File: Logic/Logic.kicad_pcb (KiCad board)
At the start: 2 copper layers, 125.4 x 128.5 mm, 65 parts, among them IC1 RPi_Pico_SMD_TH, IC2 MC74ACT05DG, J1 PJ3410, J10 PinHeader_1x03_P2.54mm_Vertic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, J2 PJ3410, J3 PJ3410, J4 PJ3410, J5 PJ3410, J6 PJ3410, J7 PJ3410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

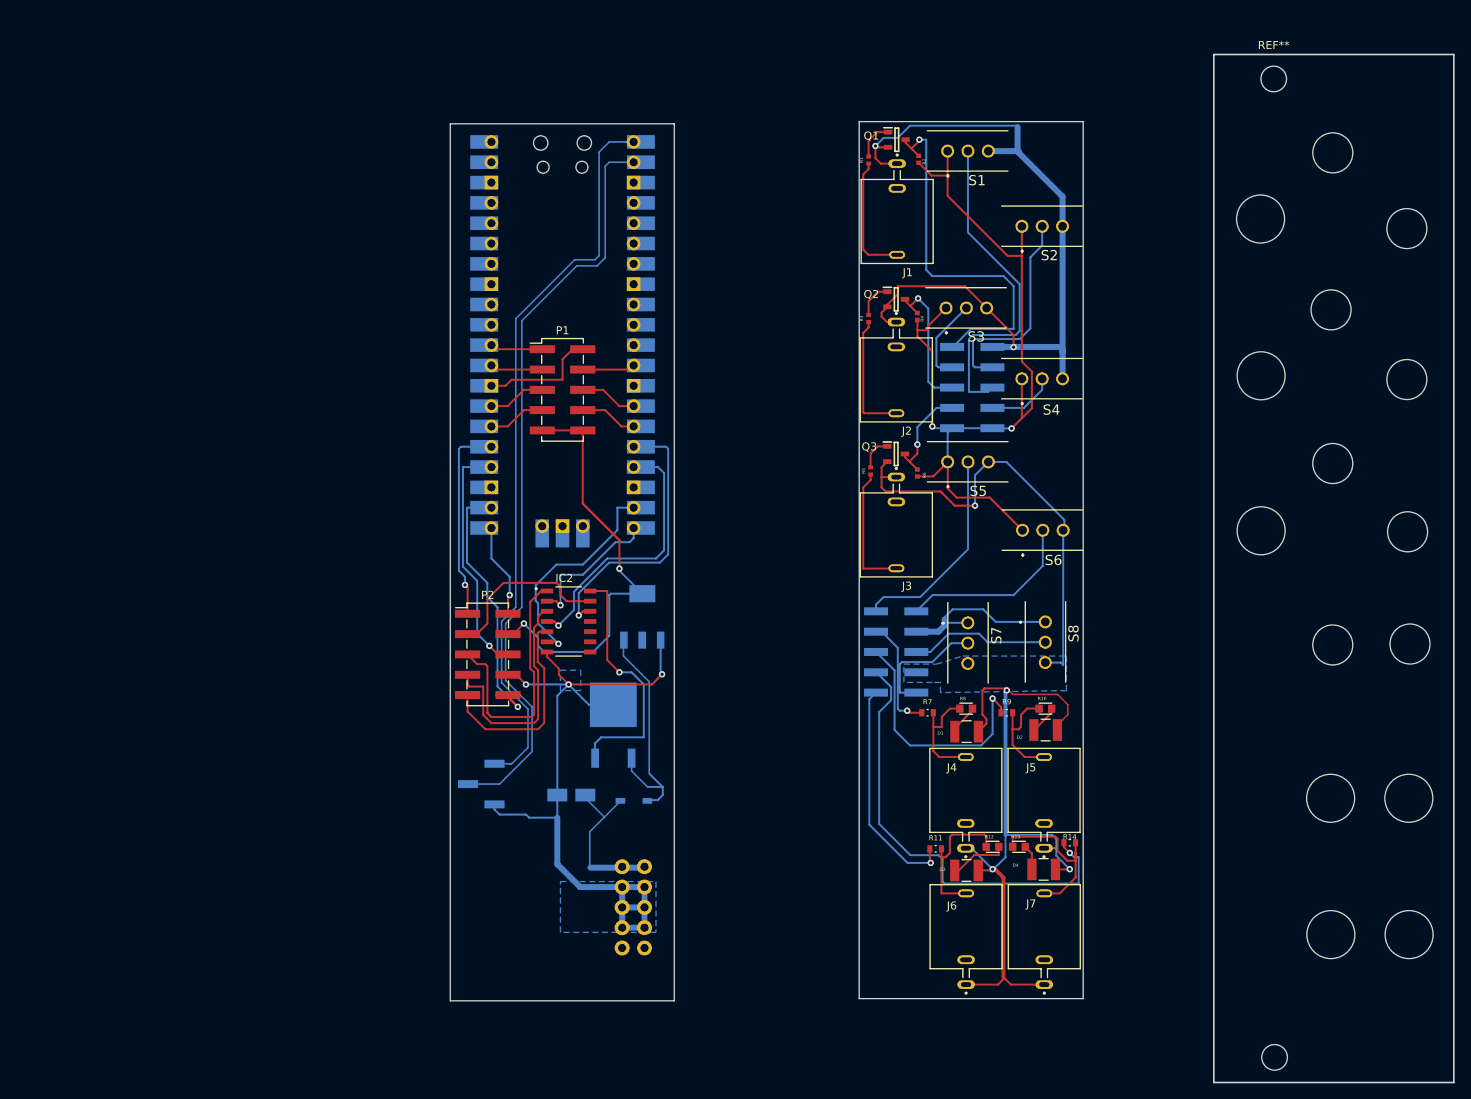
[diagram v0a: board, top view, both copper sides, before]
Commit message: Input LEDs and other tweaks
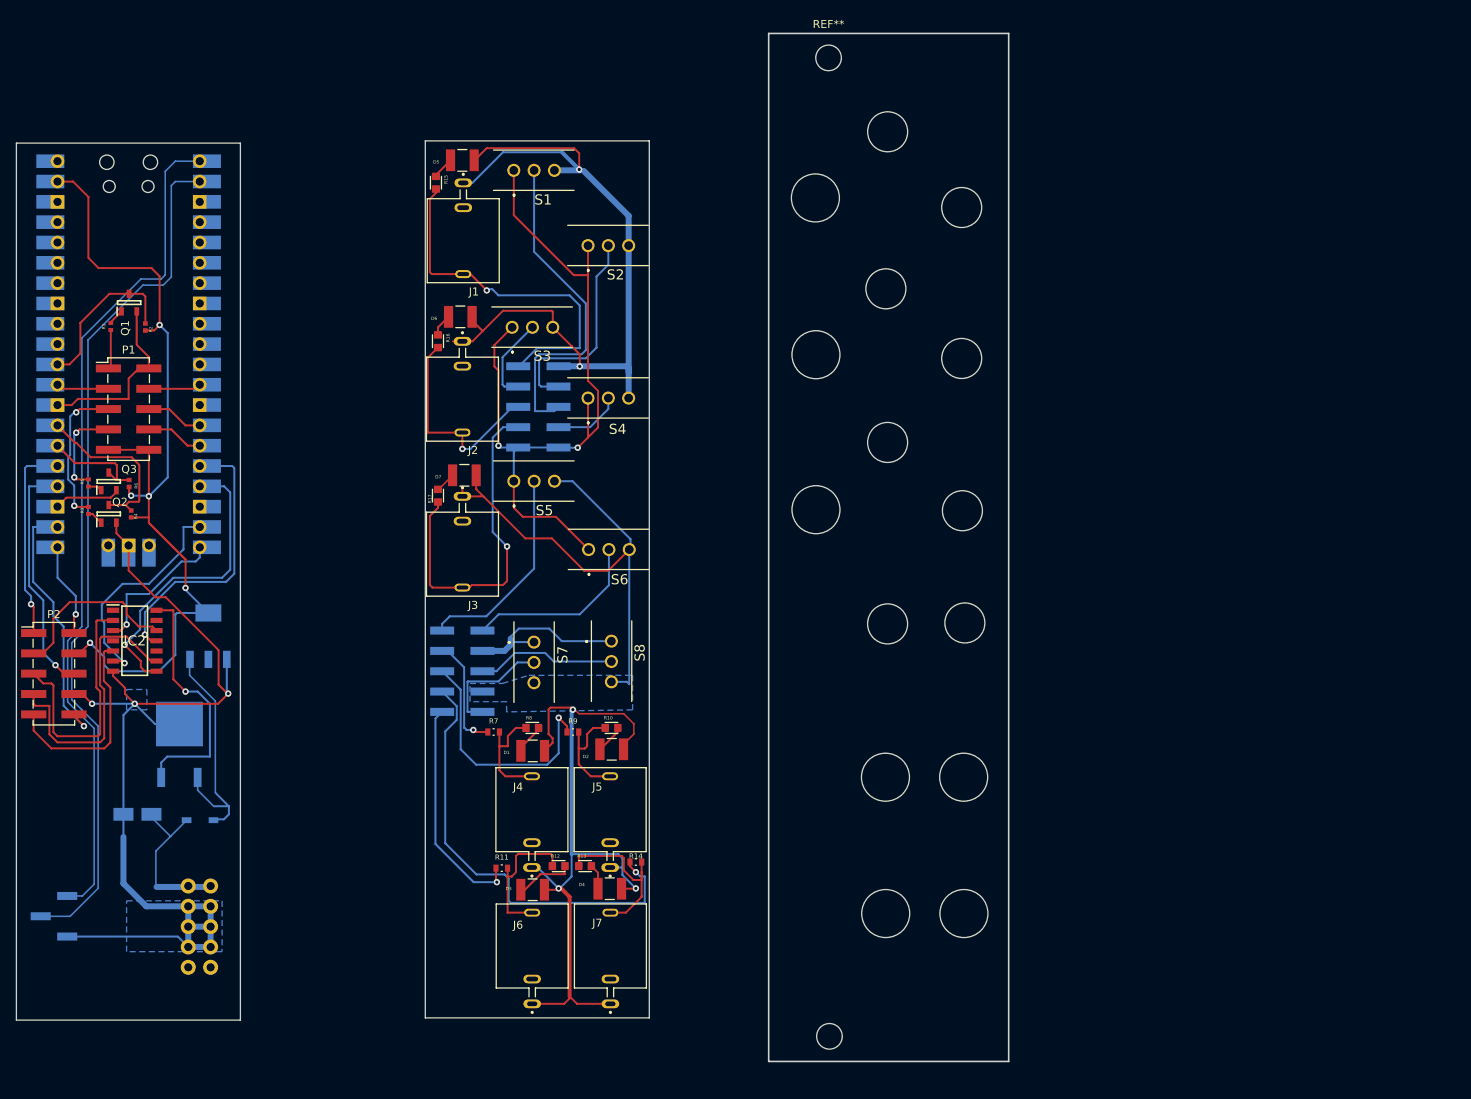
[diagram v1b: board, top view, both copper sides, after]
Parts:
- removed the D5 at (109.3, 118.7)
- added D5: LED-APD3224SURCK-F01, Import Library:LED-APD3224SURCK-F01, F.Cu at (87.8, 38.6)
- added D5: SOD3715X145N, Import Library:Diode-1N5819HW-7-F, B.Cu at (55.0, 121.1)
- added D6: LED-APD3224SURCK-F01, Import Library:LED-APD3224SURCK-F01, F.Cu at (87.6, 58.2)
- added D7: LED-APD3224SURCK-F01, Import Library:LED-APD3224SURCK-F01, F.Cu at (88.1, 78.0)
- added R15: RESC1608X50N, Import Library:RESC1608X50N, F.Cu at (84.5, 41.4)
- added R16: RESC1608X50N, Import Library:RESC1608X50N, F.Cu at (84.8, 61.2)
- added R17: RESC1608X50N, Import Library:RESC1608X50N, F.Cu at (84.8, 80.5)
- IC2: value MC74ACT05DG -> SN74HCS125QBQARQ1; footprint Import Library:MC74ACT05DG -> Import Library:SN74HCS125QBQARQ1
- moved Q2 102.0 mm to (43.6, 82.8), turned to 90 degrees
- moved R4 101.3 mm to (46.4, 82.8)
- moved R3 100.4 mm to (41.1, 82.4), turned to -90 degrees
- moved R2 98.9 mm to (48.2, 59.5)
- moved R6 98.5 mm to (46.2, 79.0)
- moved Q3 98.5 mm to (43.6, 78.8), turned to 90 degrees
- moved Q1 98.1 mm to (46.2, 56.4), turned to 90 degrees
- moved R5 97.8 mm to (41.1, 78.9), turned to -90 degrees
- moved R1 97.0 mm to (43.9, 59.4)
- moved J10 55.9 mm to (36.8, 133.1)
- moved REF** 55.7 mm to (150.5, 115.7)
- moved REF** 55.7 mm to (141.0, 96.6)
- moved REF** 55.7 mm to (141.0, 35.1)
- moved REF** 55.7 mm to (140.7, 115.7)
- moved REF** 55.7 mm to (131.9, 43.3)
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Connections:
- IC1 pad 39: (no net) -> 3.3V
- IC1 pad 42: (no net) -> Ground
- IC2 pad 1: Bus-20 -> (no net)
- IC2 pad 10: Pico -> (no net)
- IC2 pad 11: Bus -> Pico-16
- IC2 pad 12: Pico-16 -> Bus-16
- IC2 pad 13: Bus-16 -> (no net)
- IC2 pad 2: Pico-20 -> Bus-20
- IC2 pad 3: Bus-17 -> Pico-20
- IC2 pad 4: Pico-17 -> (no net)
- IC2 pad 8: Pico -> Pico-17
- IC2 pad 9: Bus -> Bus-17
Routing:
- net Ground: track 355.8 -> 416.0 mm, vias 9 -> 8
- net 3.3V: track 188.9 -> 235.7 mm, vias 4 -> 7
- net Pico-26: track 36.9 -> 69.3 mm, vias 0 -> 3
- net Pico-27: track 41.2 -> 67.1 mm, vias 0 -> 3
- net i2c-SCL: track 94.6 -> 108.2 mm
- net i2c-SDA: track 93.4 -> 105.8 mm
- net (no net): track 17.9 -> 26.0 mm
- net Pico: track 13.6 -> 5.81 mm, vias 11 -> 0
- net Pico-17: track 33.9 -> 38.0 mm, vias 0 -> 1
- net Bus-17: track 109.3 -> 113.2 mm, vias 0 -> 1
- net Bus-20: track 78.4 -> 76.4 mm, vias 0 -> 1
- net Pico-22: track 49.3 -> 47.5 mm, vias 0 -> 1
- net Pico-30: track 69.5 -> 71.3 mm, vias 0 -> 1
- net Pico-14: track 49.8 -> 48.9 mm
- net Bus-16: track 49.9 -> 50.4 mm, vias 0 -> 1
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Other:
- board size 125.4 x 128.5 mm -> 124 x 128.5 mm

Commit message: LED and cap/diode fixes
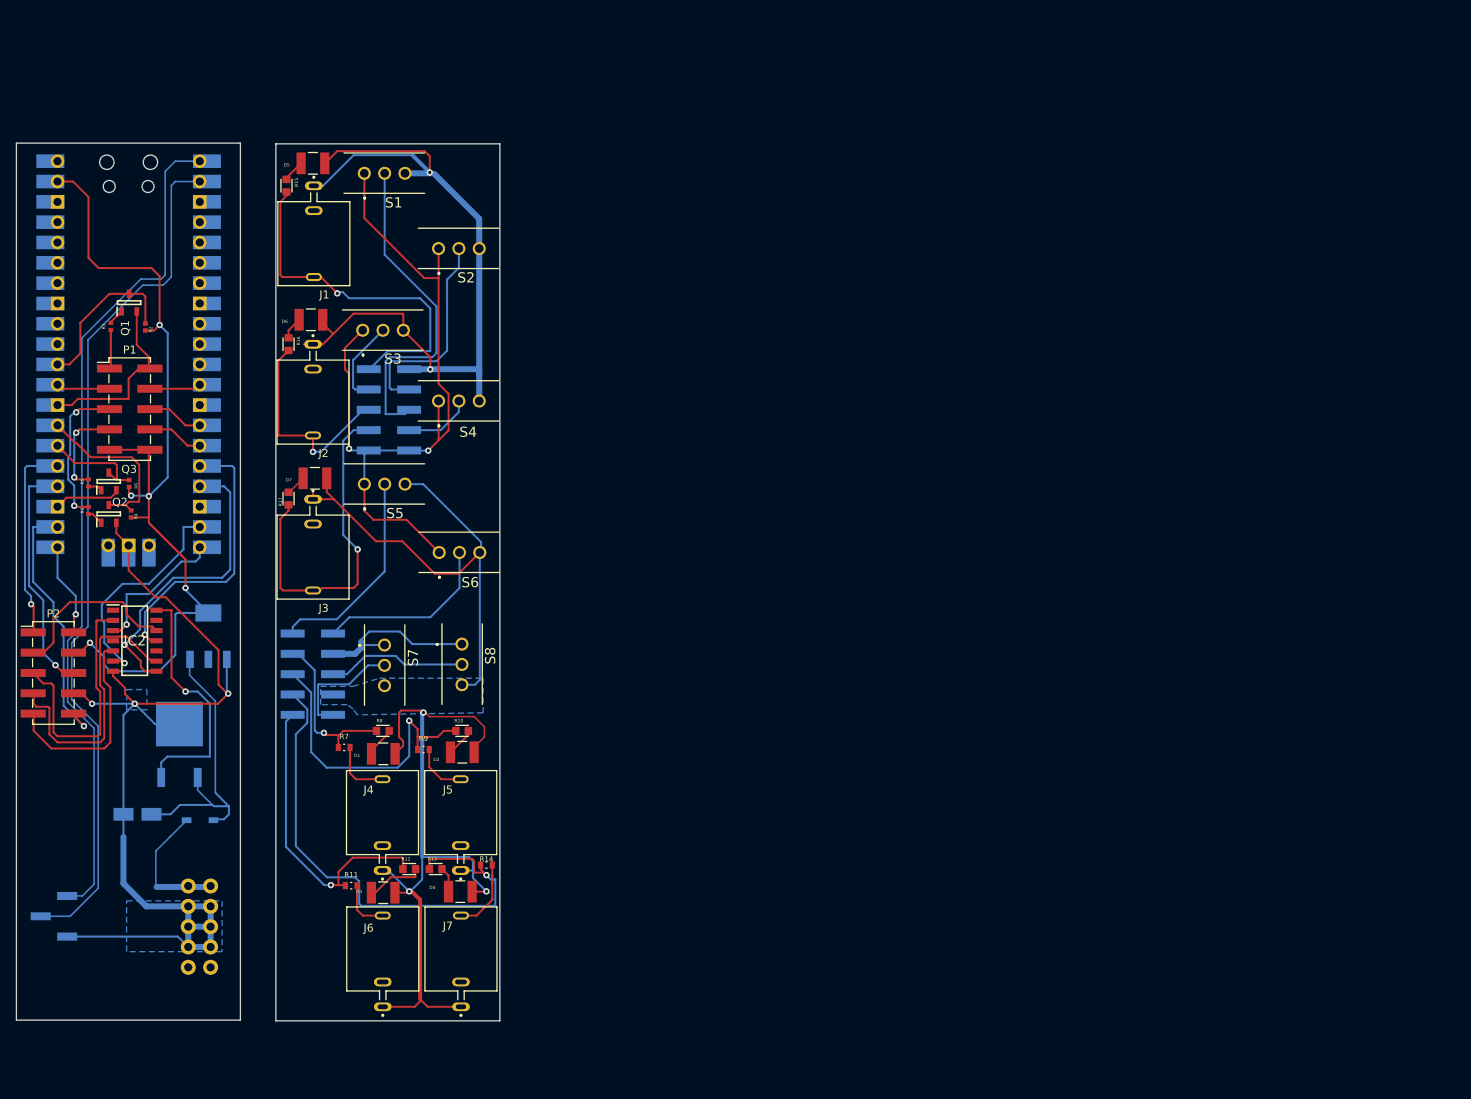
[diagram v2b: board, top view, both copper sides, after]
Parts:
- removed REF** (x8): MountingHole_5mm, MountingHole:MountingHole_5mm
- removed REF** (x7): MountingHole_6mm, MountingHole:MountingHole_6mm
- removed REF** (x2): MountingHole_3.2mm_M3, MountingHole:MountingHole_3.2mm_M3
- moved R11 18.9 mm to (73.9, 129.3)
- moved R9 18.8 mm to (82.9, 112.3)
- moved R7 18.8 mm to (73.0, 112.0)
- moved D1 18.7 mm to (77.9, 112.8)
- moved D4 18.7 mm to (87.6, 130.0)
- moved D6 18.7 mm to (68.9, 58.6)
- moved J1 18.7 mm to (69.2, 48.3)
- moved J3 18.7 mm to (69.1, 87.5)
- moved J6 18.7 mm to (77.9, 137.9)
- moved J7 18.7 mm to (87.6, 137.9)
- moved J8 18.7 mm to (69.1, 102.9)
- moved J9 18.7 mm to (78.6, 69.8)
- moved R13 18.7 mm to (84.5, 127.2)
- moved R15 18.7 mm to (65.8, 41.8)
- moved R8 18.7 mm to (77.9, 109.9)
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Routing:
- net Power: track 50.2 -> 54.9 mm
- net Bus-17: track 113.2 -> 111.4 mm
- net Bus-19: track 72.0 -> 70.3 mm
- net Ground: track 416.0 -> 415.2 mm
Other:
- board size 124 x 128.5 mm -> 60.4 x 109.7 mm

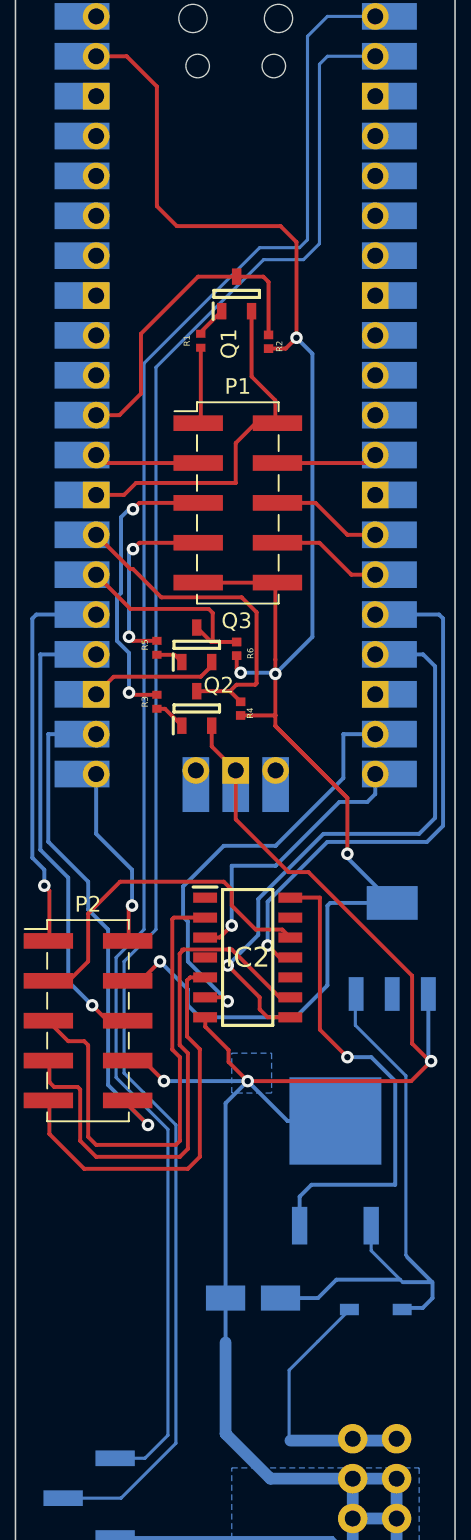
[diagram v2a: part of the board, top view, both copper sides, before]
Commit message: bus pins grounded and other little fixes
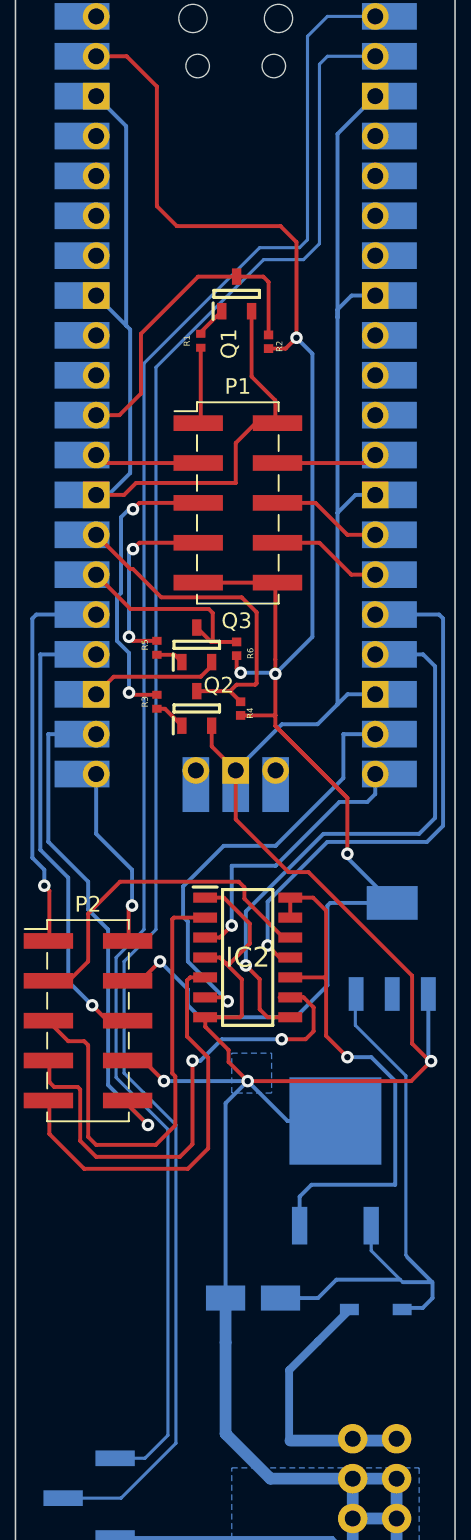
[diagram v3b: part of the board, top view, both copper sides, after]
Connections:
- IC2 pad 1: (no net) -> Ground
- IC2 pad 10: (no net) -> 5V
- IC2 pad 13: (no net) -> 5V
- IC2 pad 4: (no net) -> Ground
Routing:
- net Ground: track 415.2 -> 516.8 mm
- net 5V: track 31.3 -> 34.7 mm
- net Bus-17: track 111.4 -> 108.4 mm, vias 1 -> 3
- net Bus-20: track 76.0 -> 75.0 mm
- net Pico-17: track 38.0 -> 37.1 mm
